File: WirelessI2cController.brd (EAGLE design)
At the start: 75 x 35 mm, 38 parts, among them CN1 I2C, CN2 I2C, CN3 I2C, CN4 POWER 7.4V, IC1 FT232RQ, IC2 TC7SZ126FU, IC3 TC7SZ126FU, IC4 TWE-001L-NC, IC5 MPU-9250, IC6 MS5611-01BA03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

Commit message: 配線名を変更
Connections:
- removed net RXD2: IC4.11, RN3.6
- removed net TXD2: IC4.16, RN3.7
- new net RXD0: IC4.9, RN1.6
- new net TXD0: IC4.8, RN1.7
- net RXD1: now also IC4.11, RN3.6; no longer IC4.9, RN1.6
- net TXD1: now also IC4.16, RN3.7; no longer IC4.8, RN1.7
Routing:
- net TXD2: track 7.48 -> 0.00 mm, vias 2 -> 0
- net RXD2: track 5.94 -> 0.00 mm
- net TXD1: track 2.29 -> 7.48 mm, vias 0 -> 2
- net RXD0: track 0.00 -> 4.79 mm
- net TXD0: track 0.00 -> 2.29 mm
- net RXD1: track 4.79 -> 5.94 mm
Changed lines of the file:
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@@
 <wire x1="6.5" y1="9.25" x2="7.2" y2="9.25" width="0.2" layer="1"/>
 </signal>
-<signal name="RXD1">
+<signal name="RXD0">
 <contactref element="IC4" pad="9"/>
 <contactref element="RN1" pad="6"/>
@@
 <wire x1="27.5" y1="14.555" x2="26.9" y2="13.955" width="0.2" layer="1"/>
 </signal>
-<signal name="TXD1">
+<signal name="TXD0">
 <contactref element="IC4" pad="8"/>
 <contactref element="RN1" pad="7"/>
@@
 <wire x1="27.95" y1="31.85" x2="27.95" y2="31.7" width="0.2" layer="1"/>
 </signal>
-<signal name="RXD2">
+<signal name="RXD1">
 <contactref element="IC4" pad="11"/>
 <contactref element="RN3" pad="6"/>
@@
 <wire x1="29.5" y1="18.095" x2="29.5" y2="19.4" width="0.2" layer="1"/>
 </signal>
-<signal name="TXD2">
+<signal name="TXD1">
 <contactref element="IC4" pad="16"/>
 <contactref element="RN3" pad="7"/>

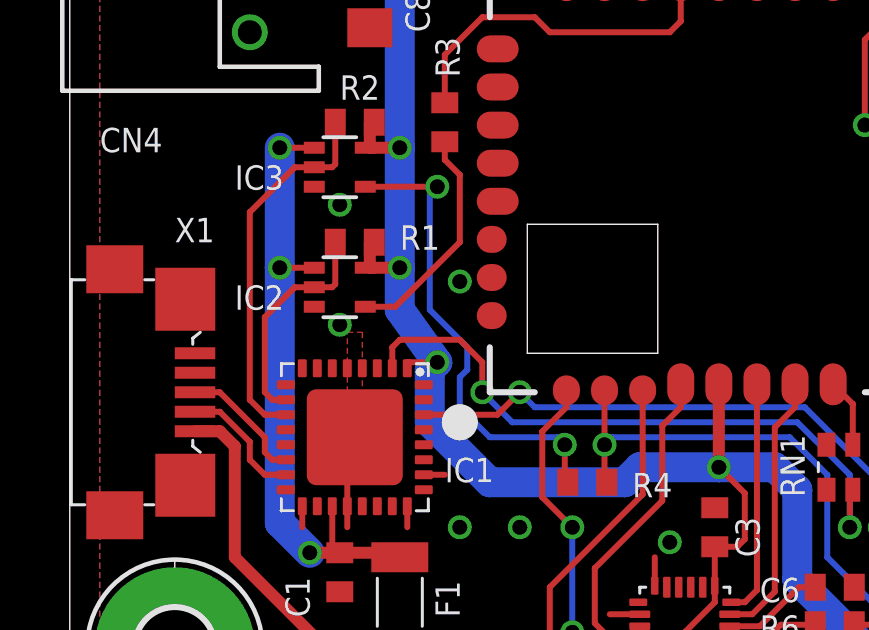
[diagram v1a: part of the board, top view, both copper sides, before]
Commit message: 電圧のシンボルを3.3Vに変更
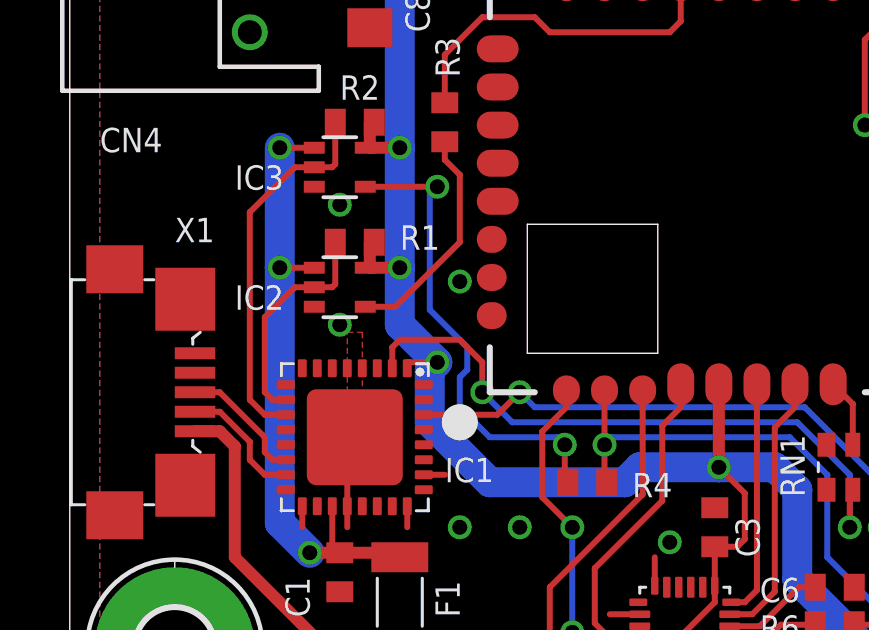
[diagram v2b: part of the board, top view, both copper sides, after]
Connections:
- net +3V renamed +3.3V
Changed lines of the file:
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@@
 <wire x1="11" y1="6.65" x2="11" y2="6.5" width="0.4" layer="1"/>
 </signal>
-<signal name="+3V">
+<signal name="+3.3V">
 <contactref element="IC1" pad="1"/>
 <contactref element="IC3" pad="5"/>
@@
 <via x="21.635" y="9.5" extent="1-16" drill="0.5"/>
 <via x="11" y="20.15" extent="1-16" drill="0.5"/>
-<wire x1="11" y1="16.15" x2="11" y2="14.75" width="1" layer="16"/>
-<wire x1="11" y1="14.75" x2="12.25" y2="13" width="1" layer="16"/>
+<wire x1="11" y1="16.15" x2="11" y2="14.25" width="1" layer="16"/>
+<wire x1="11" y1="14.25" x2="12.25" y2="13" width="1" layer="16"/>
 <wire x1="40.5" y1="14" x2="40.5" y2="15.25" width="0.4" layer="1"/>
 <via x="40.5" y="14" extent="1-16" drill="0.5"/>
